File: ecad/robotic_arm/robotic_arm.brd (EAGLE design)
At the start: 57.9 x 61.1 mm, 117 parts, among them J1 5A/28V, SW1 5A/28V, Y1 16 MHz

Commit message: Robotic Arm Rev 2: Complete ToT VR Robo Arm Rev 2.  Ready for fab.
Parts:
- added C30: 0.1uF/50V, PiB_capacitors:CAPC1005X55_SMD-0402
- added FSR_PALM: 10K, PiB_sensors:_MOLEX-0530470210_VERT_PITCH-1.25MM
- added R10: 10K, PiB_resistors:RESC1005X35_SMD-0402
- added U$17, U$18: (no value), holes:HOLE_2MM
- C11, C13, C15, C17, C9: value (none) -> 100uF/25V
- LIPO1: value 7.4V -> BATTERY_LIPO_2S_2S_7.4V_PTH-PADS_AWG-18; device PiB_batteries:BATTERY_MOLEX-89400_VERT_PITCH-2MM -> PiB_batteries:1X02_WIRE_CONNECTOR_AWG-18
- VREG-MCU: value 1A/3.3V -> TPS76833QDR 1A/3.3V
- VREG-SERVOS: value 5A/5V -> MIC29501-5.0 5A/5V
- moved JP3 18.3 mm to (11.6, 57.0), flipped to the bottom, turned to 0 degrees
- moved L2 16.3 mm to (54.9, 55.3), turned to 180 degrees
- moved C47 8.10 mm to (24.4, 51.4)
- moved C48 8.10 mm to (28.9, 51.4)
- moved C49 8.10 mm to (33.4, 51.4)
- moved C50 8.10 mm to (37.9, 51.4)
- moved C51 8.10 mm to (42.4, 51.4)
- moved FSR_INDEX 8.10 mm to (38.6, 53.8)
- moved FSR_MIDDLE 8.10 mm to (34.1, 53.8)
- moved FSR_PINKY 8.10 mm to (25.1, 53.8)
- moved FSR_RING 8.10 mm to (29.6, 53.8)
- moved FSR_THUMB 8.10 mm to (43.1, 53.8)
- moved R40 8.10 mm to (34.8, 51.4)
- moved R41 8.10 mm to (39.3, 51.4)
- moved R42 8.10 mm to (43.8, 51.4)
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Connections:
- net PB6 renamed RX_LED
- net PB7 renamed TX_LED
- net RX0 renamed RX
- net TX0 renamed TX
- removed net A0: MCU.63
- removed net A1: MCU.64
- removed net A2: MCU.1
- removed net A3: MCU.2
- removed net A4: MCU.3
- removed net A5: DEMUX1.1, MCU.4
- removed net A6: MCU.5
- removed net A7: MCU.6
- removed net PB4: MCU.40
- removed net PB5: MCU.41
- removed net PD4: MCU.29
- removed net PD5: MCU.30
- removed net PD6: MCU.31
- removed net PD7: MCU.32
- removed net PE2: DEMUX1.10, MCU.48
- removed net PE3: MCU.49
- removed net PE4: MCU.50
- removed net PE5: MCU.51
- removed net PE6: DEMUX1.11, MCU.52
- removed net PE7: DEMUX1.14, MCU.53
- removed net PG0: MCU.14
- removed net PG1: MCU.15
- removed net PG2: MCU.16
- removed net PG3: MCU.17
- removed net PG4: MCU.18
- removed net PG5: MCU.19
- removed net RX1: MCU.27
- removed net SSN: DEMUX1.13, MCU.36
- removed net TX1: MCU.28
- new net FSR_PALM: DEMUX1.4, FSR_PALM.2, R10.2
- new net S0: DEMUX1.10, MCU.50
- new net S1: DEMUX1.11, MCU.49
- new net S2: DEMUX1.14, MCU.52
- new net S3: DEMUX1.13, MCU.51
- new net SIG: DEMUX1.1, MCU.1
- net AGND: now also C30.2, R10.1; no longer DEMUX1.4
- net VSENSOR: now also C30.1, FSR_PALM.1
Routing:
- net RX: track 0.00 -> 43.8 mm, vias 0 -> 1
- net TX: track 0.00 -> 42.1 mm, vias 0 -> 1
- net FSR_PALM: track 0.00 -> 36.9 mm
- net SCK: track 0.00 -> 36.6 mm, vias 0 -> 1
- net SCL: track 0.00 -> 32.3 mm
- net SDA: track 0.00 -> 31.5 mm
- net MOSI: track 0.00 -> 31.1 mm, vias 0 -> 1
- net TX_LED: track 0.00 -> 28.1 mm, vias 0 -> 2
- net RX_LED: track 0.00 -> 28.1 mm, vias 0 -> 2
- net MISO: track 0.00 -> 27.7 mm, vias 0 -> 1
- net RESET: track 9.10 -> 34.3 mm
- net AGND: track 30.6 -> 51.7 mm, vias 32 -> 77
- net S2: track 0.00 -> 20.5 mm, vias 0 -> 2
- net S3: track 0.00 -> 20.1 mm, vias 0 -> 2
- net +: track 0.00 -> 18.9 mm
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- added copper zone on layer 1, net 3.3V
- added copper zone on layer 1, net A3.3V
- added copper zone on layer 15, net A3.3V
- added copper zone on layer 16, net A3.3V
- added copper zone on layer 1, net AGND
- added copper zone on layer 15, net GND
- added copper zone on layer 16, net GND
- added copper zone on layer 1, net N$1
- added copper zone on layer 16, net N$1
- added copper zone on layer 2, net N$1
- added copper zone on layer 1, net N$39
- added copper zone on layer 16, net VSENSOR
- removed copper zone on layer 15, net GARBAGE
- removed copper zone on layer 2, net GARBAGE
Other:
- board text removed: "Transmission of Touch VR Robotic Arm Rev 1"

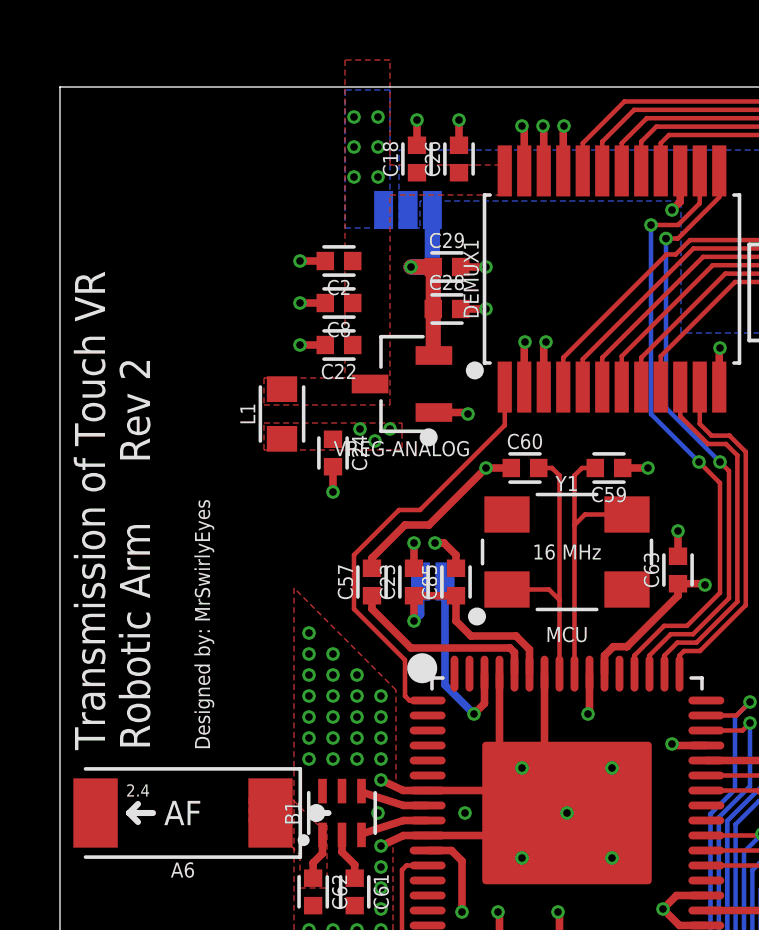
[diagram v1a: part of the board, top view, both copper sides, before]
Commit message: Rev 3: Robotic Arm.  Fix mistake with A3.3V not connected to ATMEGA128RFA1 EVDD (pin 59) which may be affecting the bootload process.
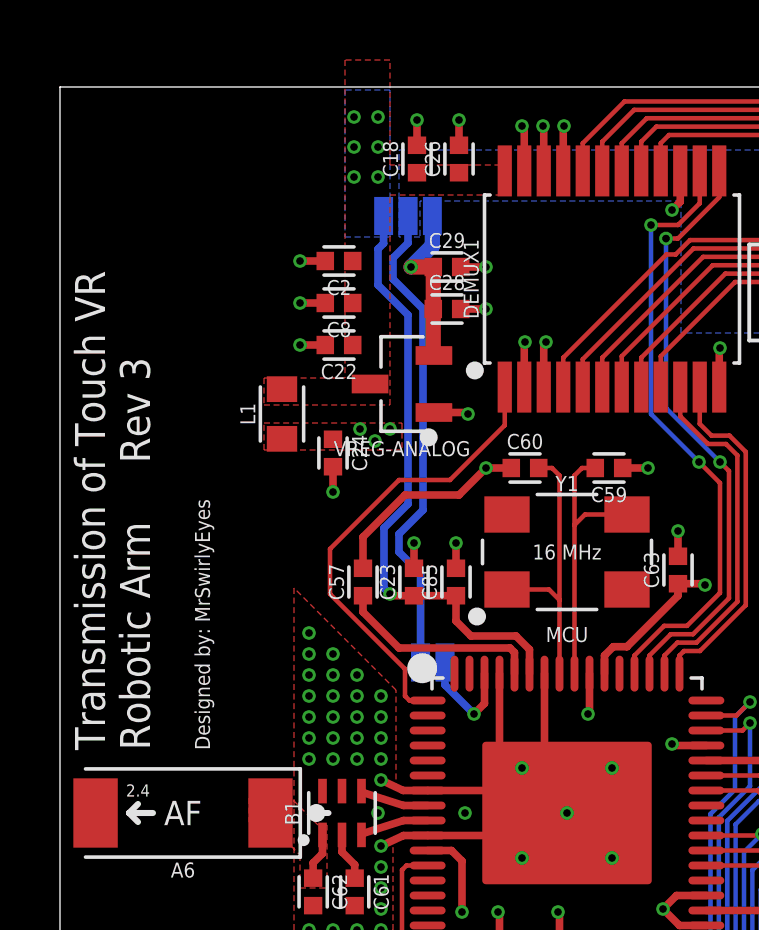
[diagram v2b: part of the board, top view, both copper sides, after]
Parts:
- moved JP2 2.70 mm to (12.4, 41.9)
- moved C57 0.30 mm to (10.1, 44.6)
- moved JP3 0.20 mm to (11.6, 56.8)
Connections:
- net N$12 renamed AREF
- removed net AVCC: C23.1, C85.1, JP2.1, MCU.59
- removed net VCC: JP1.VCC
- net A3.3V: now also C23.1, C85.1, MCU.59
- net VSENSOR: now also JP2.1
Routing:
- net A3.3V: track 10.0 -> 30.3 mm, vias 6 -> 7
- net VSENSOR: track 11.8 -> 28.0 mm
- net AVCC: track 8.14 -> 0.00 mm, vias 1 -> 0
- net AREF: track 6.31 -> 3.61 mm
- net SIG: track 14.3 -> 15.6 mm
- net GND: track 52.5 -> 53.2 mm
- net A1.8V: track 6.33 -> 5.72 mm
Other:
- board text added: "Transmission of Touch VR Robotic Arm Rev 3"
- board text removed: "Transmission of Touch VR Robotic Arm Rev 2"

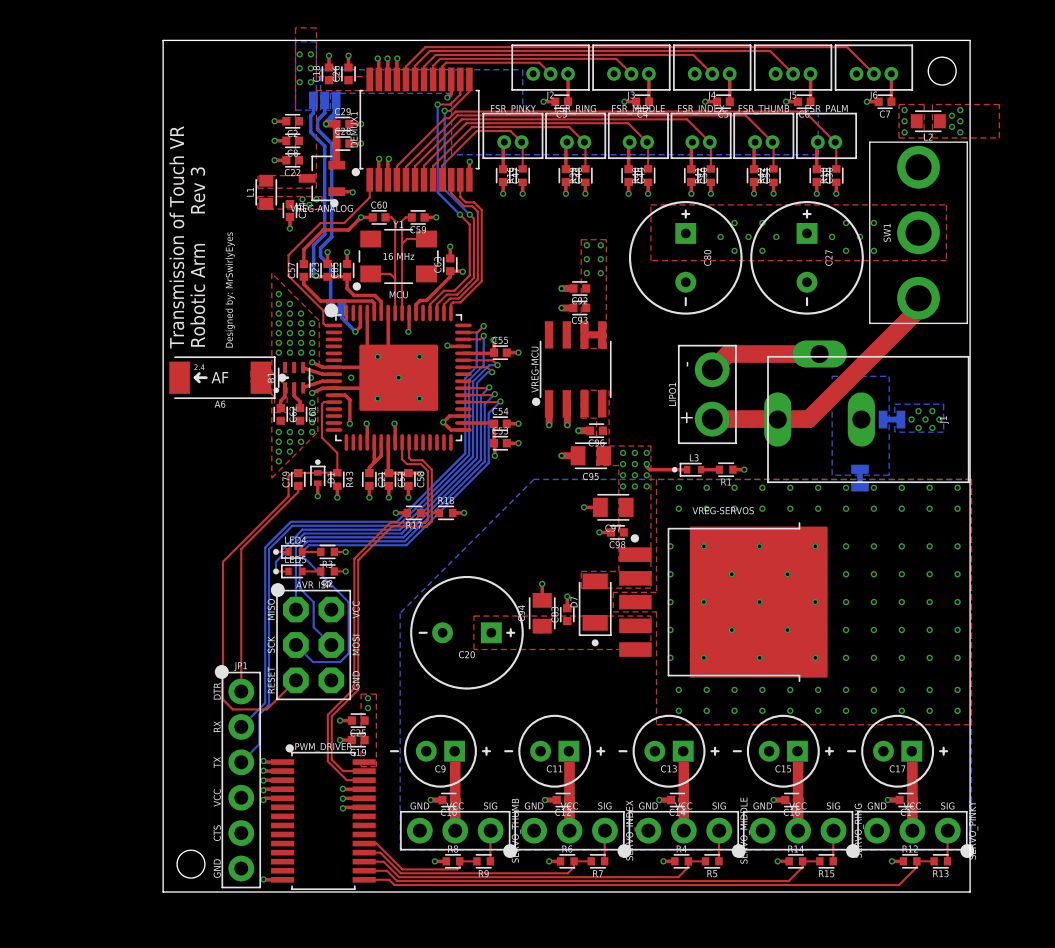
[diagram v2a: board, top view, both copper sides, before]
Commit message: Updated aesthetics of robotic arm board.  Changed orientation.
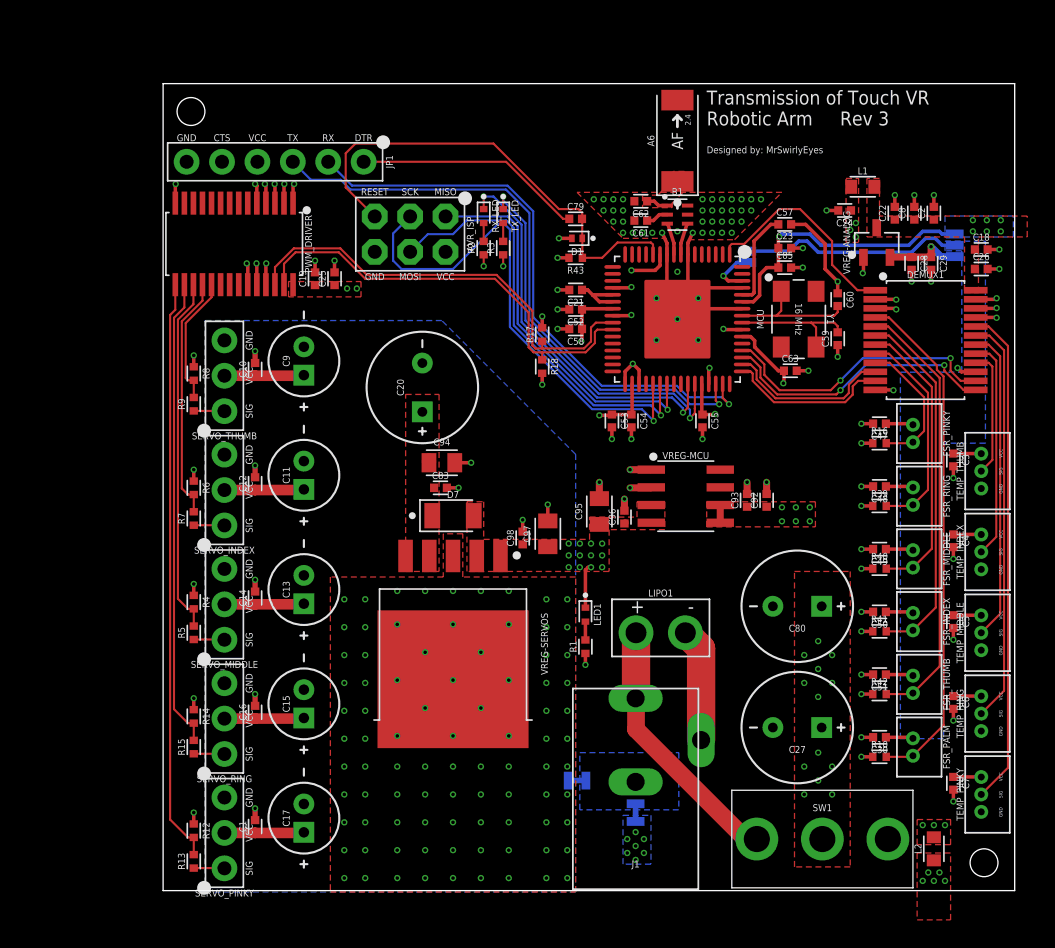
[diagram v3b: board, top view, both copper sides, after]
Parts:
- removed J2, J3, J4, J5, J6: (no value), PiB_connectors:_MOLEX-0530470310_VERT_PITCH-1.25MM
- removed L3: BLUE, PiB_leds:LEDC1005X40_LED-0402
- removed LED4: GREEN, PiB_leds:LEDC1005X40_LED-0402
- removed LED5: RED, PiB_leds:LEDC1005X40_LED-0402
- added LED1: BLUE, PiB_leds:LEDC1005X40_LED-0402
- added RX_LED: RED, PiB_leds:LEDC1005X40_LED-0402
- added TEMP_INDEX, TEMP_MIDDLE, TEMP_PINKY, TEMP_RING, TEMP_THUMB: TMP36, PiB_sensors:_MOLEX-0530470310_VERT_PITCH-1.25MM
- added TX_LED: GREEN, PiB_leds:LEDC1005X40_LED-0402
- added U$20: (no value), PiB_logo:MRSWIRLYEYES-LOGO
- added U$21: (no value), PiB_logo:LRG-LOGO
- LIPO1: value BATTERY_LIPO_2S_2S_7.4V_PTH-PADS_AWG-18 -> LIPO 2S
- R17, R18: value 10K -> 4.7K
- moved U$17 56.9 mm to (58.9, 2.10), turned to 270 degrees
- moved U$18 54.0 mm to (2.00, 56.0), turned to 270 degrees
- moved R13 53.6 mm to (2.20, 2.20), turned to 90 degrees
- moved L2 52.2 mm to (55.3, 3.10), turned to 90 degrees
- moved SERVO_PINKY 52.0 mm to (4.40, 1.70), turned to 90 degrees
- moved R12 51.4 mm to (2.20, 4.40), turned to 270 degrees
- moved C7 49.1 mm to (56.7, 7.80), turned to 270 degrees
- moved C18 48.5 mm to (58.7, 46.1), turned to 0 degrees
- moved C26 47.5 mm to (58.7, 44.7), turned to 0 degrees
- moved C1 46.7 mm to (6.60, 4.70), turned to 90 degrees
- moved C2 46.5 mm to (55.3, 48.7), turned to 90 degrees
- moved JP3 46.4 mm to (56.8, 46.4), turned to 90 degrees
- moved R15 46.1 mm to (2.20, 10.4), turned to 90 degrees
- moved C8 44.9 mm to (53.9, 48.7), turned to 90 degrees
- moved R14 44.4 mm to (2.20, 12.6), turned to 270 degrees
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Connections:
- removed net N$42: JP1.CTS
- net A3.3V: now also TEMP_INDEX.VCC, TEMP_MIDDLE.VCC, TEMP_PINKY.VCC, TEMP_RING.VCC, TEMP_THUMB.VCC; no longer J2.3, J3.3, J4.3, J5.3, J6.3
- net AGND: now also TEMP_INDEX.GND, TEMP_MIDDLE.GND, TEMP_PINKY.GND, TEMP_RING.GND, TEMP_THUMB.GND; no longer J2.1, J3.1, J4.1, J5.1, J6.1
- net N$2: now also LED1.K; no longer L3.K
- net N$3: now also TX_LED.K; no longer LED4.K
- net N$5: now also RX_LED.K; no longer LED5.K
- net RX_LED: now also RX_LED.A; no longer LED5.A
- net TEMP_INDEX: now also TEMP_INDEX.SIG; no longer J3.2
- net TEMP_MIDDLE: now also TEMP_MIDDLE.SIG; no longer J4.2
- net TEMP_PINKY: now also TEMP_PINKY.SIG; no longer J6.2
- net TEMP_RING: now also TEMP_RING.SIG; no longer J5.2
- net TEMP_THUMB: now also TEMP_THUMB.SIG; no longer J2.2
- net TX_LED: now also TX_LED.A; no longer LED4.A
- net VBAT: now also LED1.A; no longer L3.A
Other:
- board size 57.9 x 61.1 mm -> 61.1 x 57.9 mm

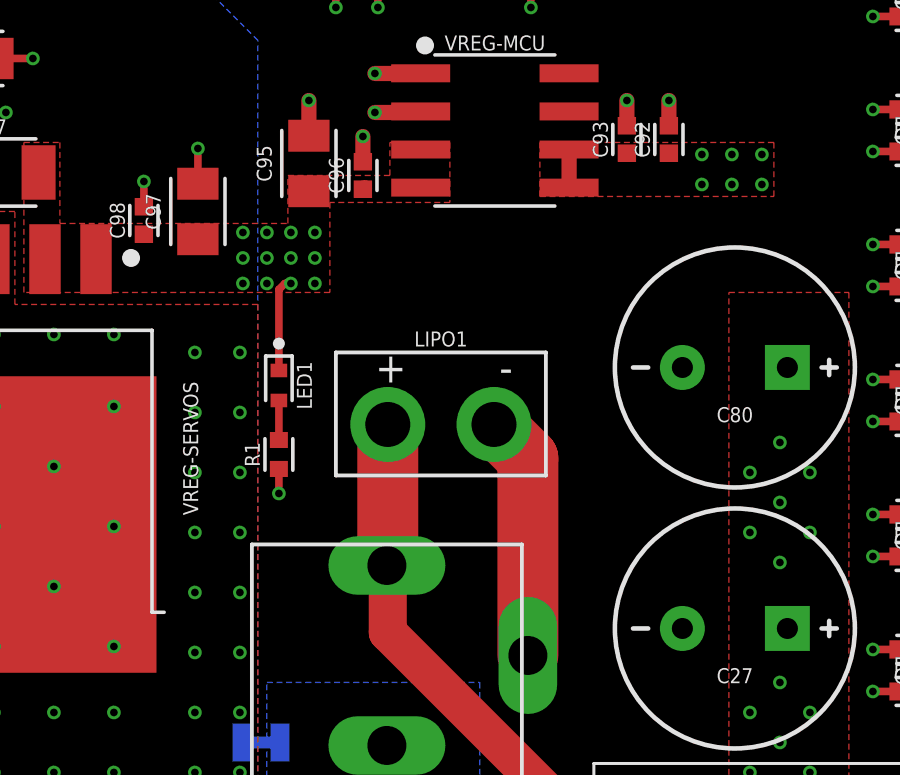
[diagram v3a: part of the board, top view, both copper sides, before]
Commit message: Rev 3: Changes to robotic and and touch glove to fix inconsistencies and errors from Rev 2.
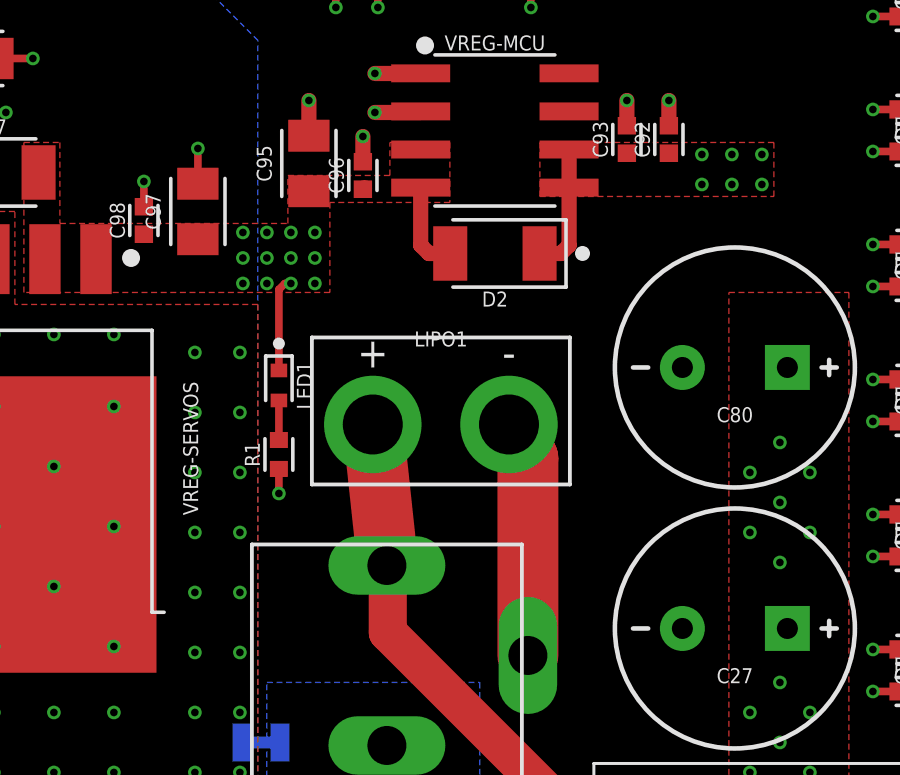
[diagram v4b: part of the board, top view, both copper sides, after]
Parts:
- added D2: 1A/50V, PiB_discrete_semiconductors:SODFL3516X170
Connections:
- net 3.3V: now also D2.A
- net VBAT: now also D2.K
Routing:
- net VBAT: track 3.30 -> 6.36 mm
- net 3.3V: track 22.1 -> 25.1 mm
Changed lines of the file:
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@@
 <element name="U$20" library="PiB_logo" package="MRSWIRLYEYES-LOGO" value="" x="26" y="33" smashed="yes" rot="MR0"/>
 <element name="U$21" library="PiB_logo" package="LRG-LOGO" value="" x="20.9" y="5.3" smashed="yes" rot="MR0"/>
+<element name="D2" library="PiB_discrete_semiconductors" package="SODFL3516X170" package3d_urn="urn:adsk.eagle:package:2939213/1" value="1A/50V" x="37.5" y="24.3" smashed="yes" rot="R180">
+<attribute name="DATASHEET" value="http://www.comchiptech.com/cms/UserFiles/CGRKM4001-HF%20Thru.%20CGRKM4007-HF%20RevG.pdf" x="37.5" y="24.3" size="1.778" layer="27" rot="R180" display="off"/>
+<attribute name="DIST" value="Digikey" x="37.5" y="24.3" size="1.778" layer="27" rot="R180" display="off"/>
+<attribute name="DISTLINK" value="https://www.digikey.com/products/en?keywords=641-1511-1-ND" x="37.5" y="24.3" size="1.778" layer="27" rot="R180" display="off"/>
+<attribute name="DISTPN" value="641-1511-1-ND" x="37.5" y="24.3" size="1.778" layer="27" rot="R180" display="off"/>
+<attribute name="MFR" value="Comchip Technology" x="37.5" y="24.3" size="1.778" layer="27" rot="R180" display="off"/>
+<attribute name="MPN" value="CGRKM4001-HF" x="37.5" y="24.3" size="1.778" layer="27" rot="R180" display="off"/>
+<attribute name="NAME" x="37.5" y="23.03" size="0.5" layer="25" font="vector" ratio="10" rot="R180" align="bottom-center"/>
+<attribute name="VALUE" x="37.5" y="25.57" size="0.25" layer="27" font="vector" ratio="10" rot="R180" align="top-center"/>
+</element>
 </elements>
 <signals>
@@
 <contactref element="SW1" pad="S1"/>
 <contactref element="LIPO1" pad="+"/>
-<wire x1="33.93" y1="18.6" x2="33.93" y2="13.93" width="2.032" layer="1"/>
+<wire x1="33.43" y1="18.6" x2="33.93" y2="13.93" width="2.032" layer="1"/>
 <wire x1="33.93" y1="13.93" x2="33.9" y2="13.9" width="1.27" layer="1"/>
 <wire x1="42.6" y1="3.8" x2="41.8" y2="3.8" width="1.27" layer="1"/>
@@
 <contactref element="J1" pad="GND_BATTERY"/>
 <contactref element="LIPO1" pad="-"/>
-<wire x1="37.47" y1="18.6" x2="38.6" y2="17.47" width="2.032" layer="1"/>
+<wire x1="37.97" y1="18.6" x2="38.6" y2="17.47" width="2.032" layer="1"/>
 <wire x1="38.6" y1="17.47" x2="38.6" y2="10.9" width="2.032" layer="1"/>
 </signal>
@@
 <via x="13.2" y="43.3" extent="1-16" drill="0.254"/>
 <via x="13.9" y="43.3" extent="1-16" drill="0.254"/>
+<contactref element="D2" pad="A"/>
+<wire x1="39.9734" y1="26.495" x2="39.9734" y2="24.5734" width="0.508" layer="1"/>
+<wire x1="39.9734" y1="24.5734" x2="39.7" y2="24.3" width="0.508" layer="1"/>
+<wire x1="39.7" y1="24.3" x2="38.9894" y2="24.3" width="0.508" layer="1"/>
 </signal>
 <signal name="VSENSOR">
@@
 <vertex x="32" y="23"/>
 </polygon>
+<contactref element="D2" pad="K"/>
+<wire x1="35" y1="26.4684" x2="35.0266" y2="26.495" width="0.508" layer="1"/>
+<wire x1="35.0266" y1="26.495" x2="35.0266" y2="24.5734" width="0.508" layer="1"/>
+<wire x1="35.0266" y1="24.5734" x2="35.3" y2="24.3" width="0.508" layer="1"/>
+<wire x1="35.3" y1="24.3" x2="36.0106" y2="24.3" width="0.508" layer="1"/>
 </signal>
 <signal name="N$1">
